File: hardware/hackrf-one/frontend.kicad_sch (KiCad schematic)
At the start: 149 parts, among them J10 GND_CLIP, J2 RF-SHIELD-FRAME, J3 RF-SHIELD-COVER, J4 MOUNTING_HOLE, J5 MOUNTING_HOLE, J6 MOUNTING_HOLE, J7 MOUNTING_HOLE, J8 MOUNTING_HOLE, J9 MOUNTING_HOLE, P13 GPO1, P17 GPO6, P19 GPO3, P21 REF_IN, P27 MIXER_SDATA, P31 MIXER_SCLK, P32 MIXER_ENX, P33 MIXER_RESETX, P34 MIX_BYPASS, P35 !MIX_BYPASS, P4 ANTENNA, P43 RX, P44 HP, P45 LP, P46 TX_MIX_BP, P47 RX_MIX_BP, P48 TX_AMP, P49 RX_AMP, P50 AMP_BYPASS, P51 !TX_AMP_PWR, P52 !RX_AMP_PWR, P6 GPO4, P7 GPO2, Q4 MOSFET_P, T1 MIX_IN_BALUN, T2 MIX_OUT_BALUN, U1 SKY13453, U10 SKY13453, U11 SKY13453, U12 SKY13317, U13 TRF37B73, U14 SKY13317, U2 SKY13453, U25 TRF37B73, U3 RX_LOWPASS_FILTER, U4 RFFC5072, U5 SKY13453, U6 SKY13453, U7 SKY13453, U8 RX_HIGHPASS_FILTER, U9 SKY13317

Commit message: Fixed minor DRCs
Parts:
- P4: footprint hackrf:GSG-SMA-73251-2120 -> gsg-modules:SMA-73251-2120
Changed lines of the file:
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@@
 			)
 		)
-		(property "Footprint" "hackrf:GSG-SMA-73251-2120"
+		(property "Footprint" "gsg-modules:SMA-73251-2120"
 			(at 414.02 214.63 0)
 			(effects

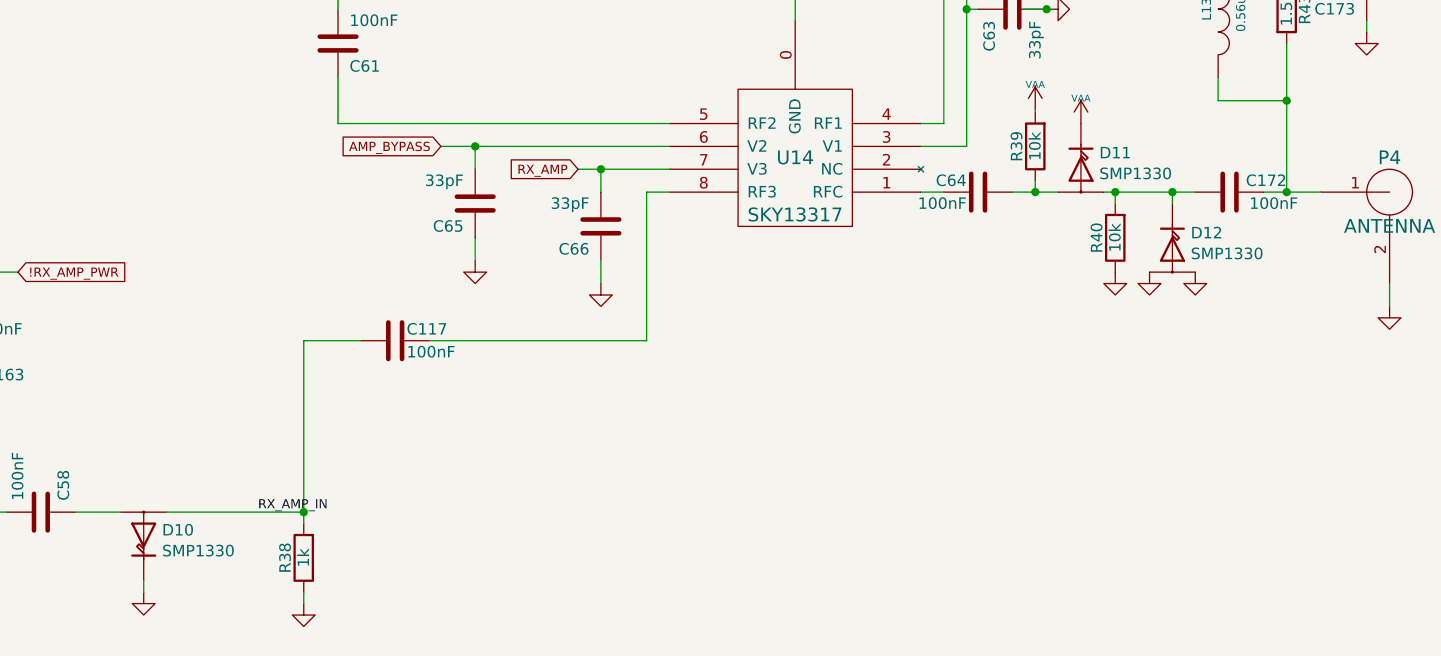
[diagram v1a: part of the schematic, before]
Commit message: Changed from SMP1330 to CLA4611 to improve performance to 6GHz
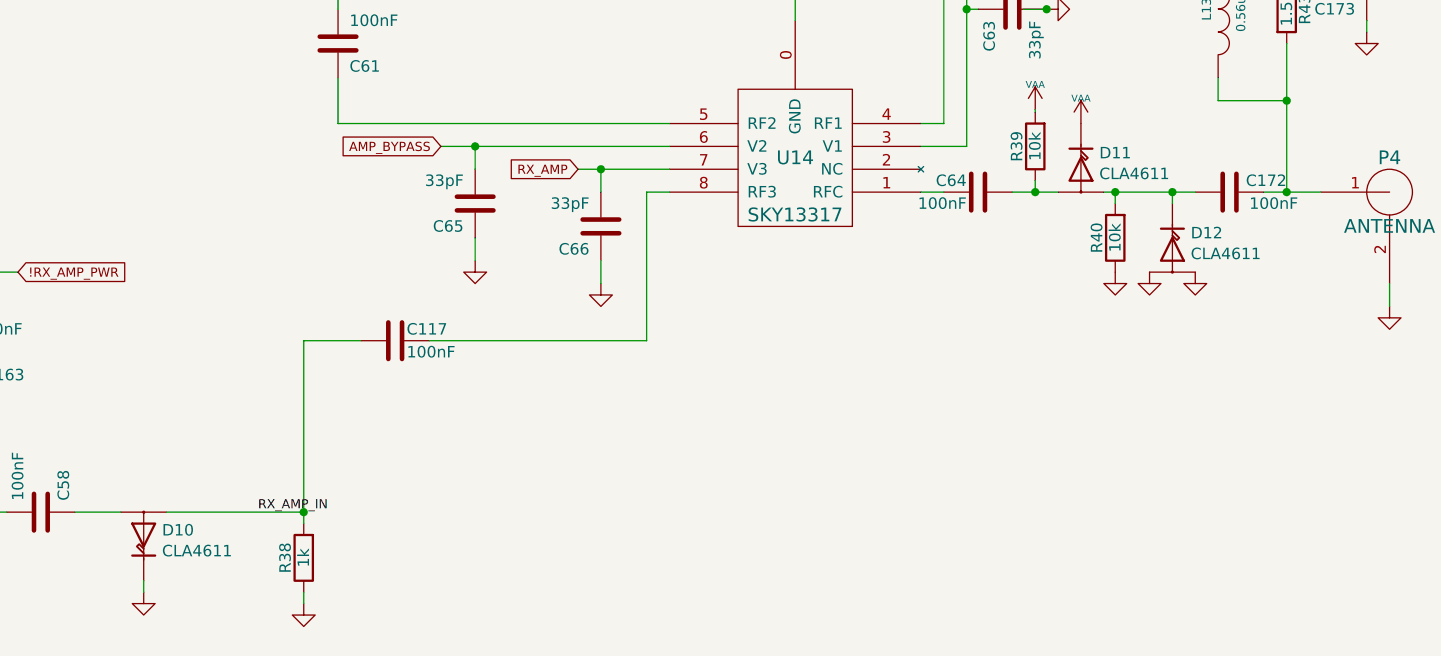
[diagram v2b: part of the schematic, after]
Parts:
- D10, D11, D12: value SMP1330 -> CLA4611; footprint gsg-modules:SMP1330-085LF -> gsg-modules:SkyworksLimiterDiode; symbol hackrf-one:D_Limiter_DualAn-hackrf -> gsg-kicad-lib:CLA4611_Limiter_Diode; Part Number SMP1330-085LF -> CLA4611-085LF
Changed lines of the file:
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@@
 	)
 	(symbol
-		(lib_id "hackrf-one:D_Limiter_DualAn-hackrf")
+		(lib_id "gsg-kicad-lib:CLA4611_Limiter_Diode")
 		(at 379.73 212.09 270)
 		(unit 1)
@@
 			)
 		)
-		(property "Value" "SMP1330"
+		(property "Value" "CLA4611"
 			(at 381.762 212.598 90)
 			(effects
@@
 			)
 		)
-		(property "Footprint" "gsg-modules:SMP1330-085LF"
+		(property "Footprint" "gsg-modules:SkyworksLimiterDiode"
 			(at 379.73 212.09 0)
 			(effects
@@
 		)
 		(property "Description" "Limiter Diode"
-			(at 379.73 212.09 90)
+			(at 379.73 212.09 0)
 			(effects
 				(font
@@
 			)
 		)
-		(property "Part Number" "SMP1330-085LF"
+		(property "Part Number" "CLA4611-085LF"
 			(at 379.73 212.09 90)
 			(effects
@@
 	)
 	(symbol
-		(lib_id "hackrf-one:D_Limiter_DualAn-hackrf")
+		(lib_id "gsg-kicad-lib:CLA4611_Limiter_Diode")
 		(at 389.89 220.98 270)
 		(unit 1)
@@
 			)
 		)
-		(property "Value" "SMP1330"
+		(property "Value" "CLA4611"
 			(at 391.922 221.488 90)
 			(effects
@@
 			)
 		)
-		(property "Footprint" "gsg-modules:SMP1330-085LF"
+		(property "Footprint" "gsg-modules:SkyworksLimiterDiode"
 			(at 389.89 220.98 0)
 			(effects
@@
 		)
 		(property "Description" "Limiter Diode"
-			(at 389.89 220.98 90)
+			(at 389.89 220.98 0)
 			(effects
 				(font
@@
 			)
 		)
-		(property "Part Number" "SMP1330-085LF"
+		(property "Part Number" "CLA4611-085LF"
 			(at 389.89 220.98 90)
 			(effects
@@
 	)
 	(symbol
-		(lib_id "hackrf-one:D_Limiter_DualAn-hackrf")
+		(lib_id "gsg-kicad-lib:CLA4611_Limiter_Diode")
 		(at 275.59 252.73 90)
 		(unit 1)
@@
 			)
 		)
-		(property "Value" "SMP1330"
+		(property "Value" "CLA4611"
 			(at 277.622 254.508 90)
 			(effects
@@
 			)
 		)
-		(property "Footprint" "gsg-modules:SMP1330-085LF"
+		(property "Footprint" "gsg-modules:SkyworksLimiterDiode"
 			(at 275.59 252.73 0)
 			(effects
@@
 		)
 		(property "Description" "Limiter Diode"
-			(at 275.59 252.73 90)
+			(at 275.59 252.73 0)
 			(effects
 				(font
@@
 			)
 		)
-		(property "Part Number" "SMP1330-085LF"
+		(property "Part Number" "CLA4611-085LF"
 			(at 275.59 252.73 90)
 			(effects

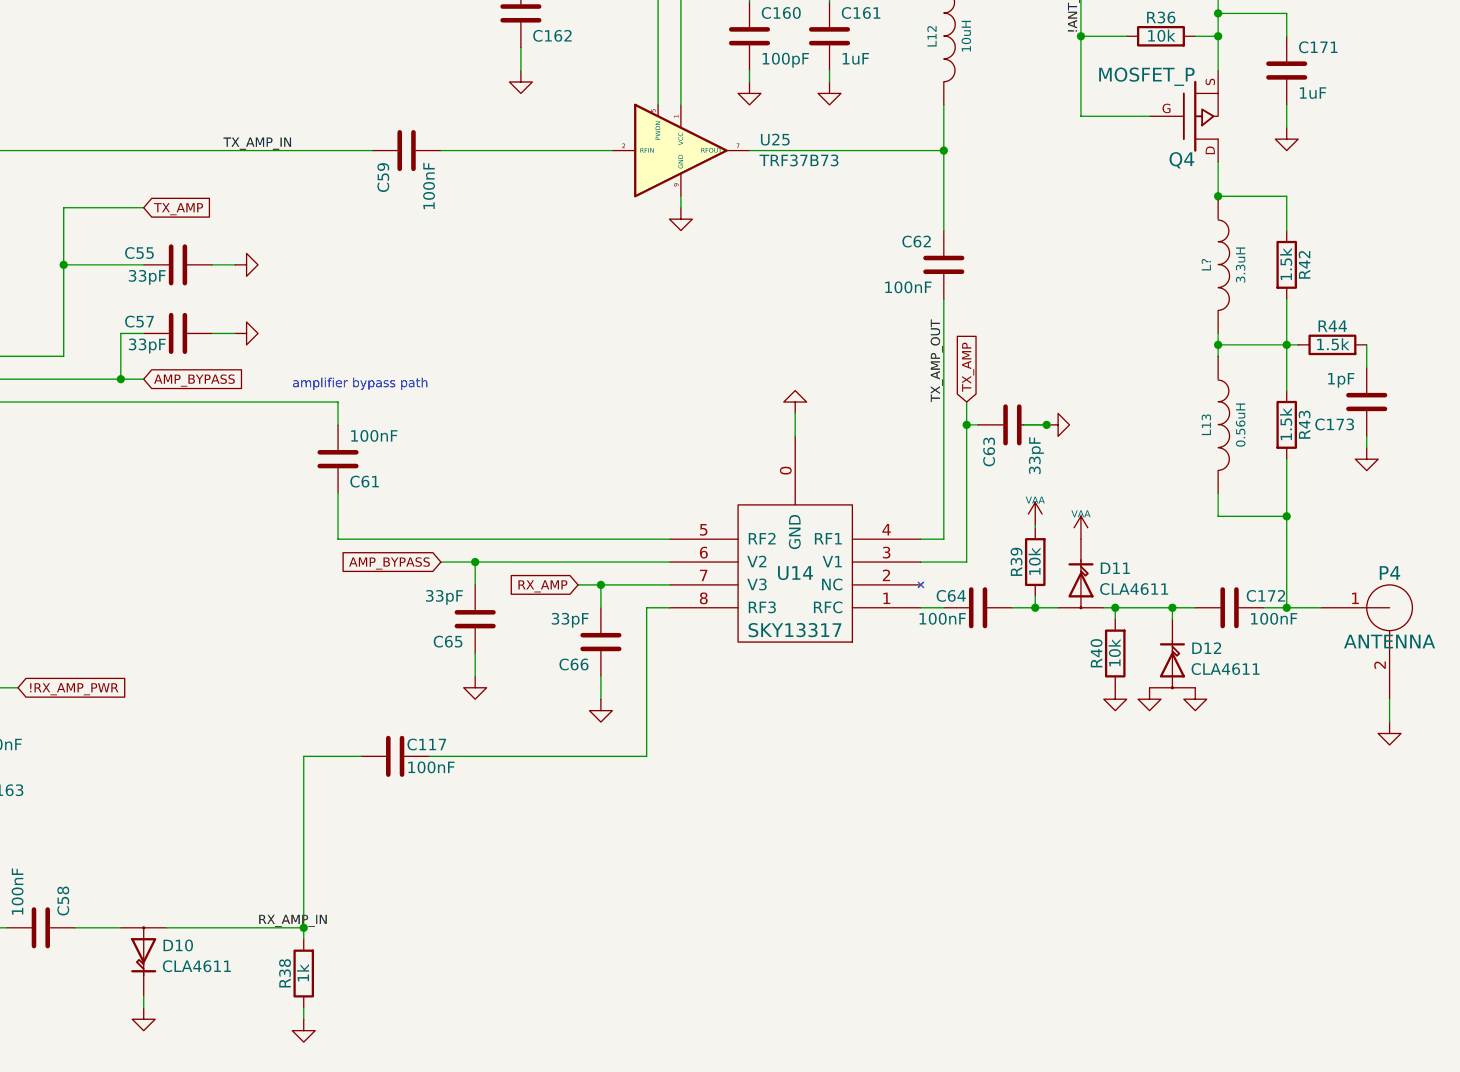
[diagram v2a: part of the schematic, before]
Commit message: Changed limiter to CLA4611. Added Schottky bias tee diode
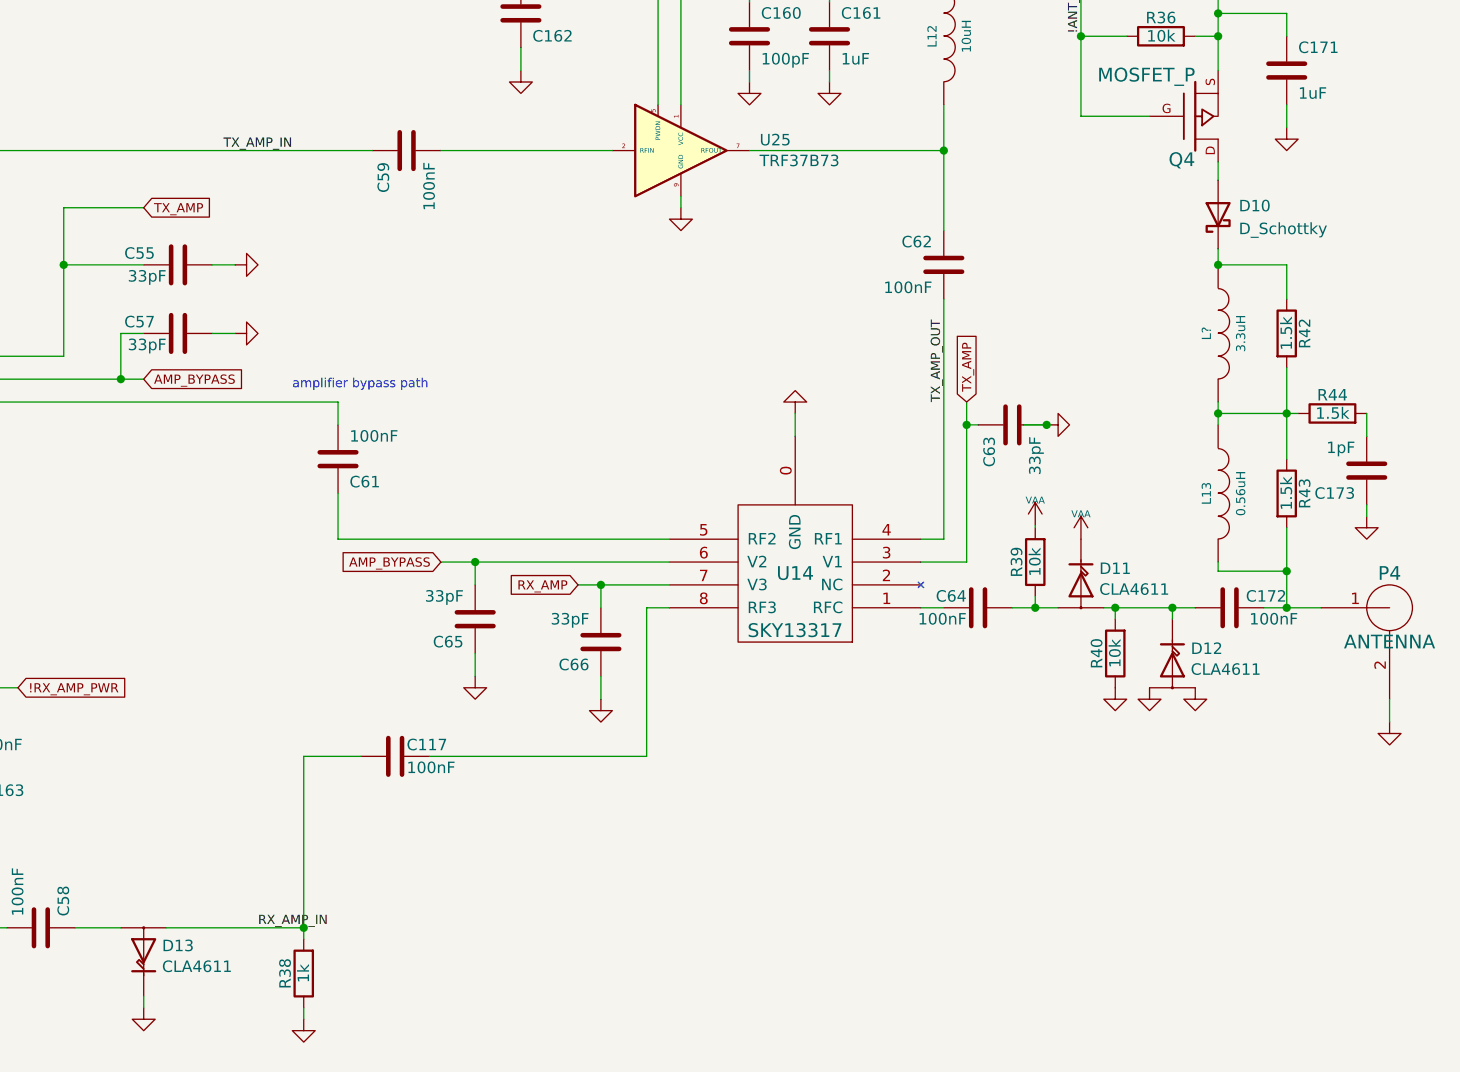
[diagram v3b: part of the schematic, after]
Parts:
- added D10: D_Schottky, gsg-modules:DSN1006-2, symbol Device:D_Schottky
- renumbered D10 to D13
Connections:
- net at L?.1, R42.1: now also D10.1 (K); no longer Q4.D
- new net: D10.2 (A), Q4.D
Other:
- moved on the sheet: C173, L13, L?, R42, R43, R44

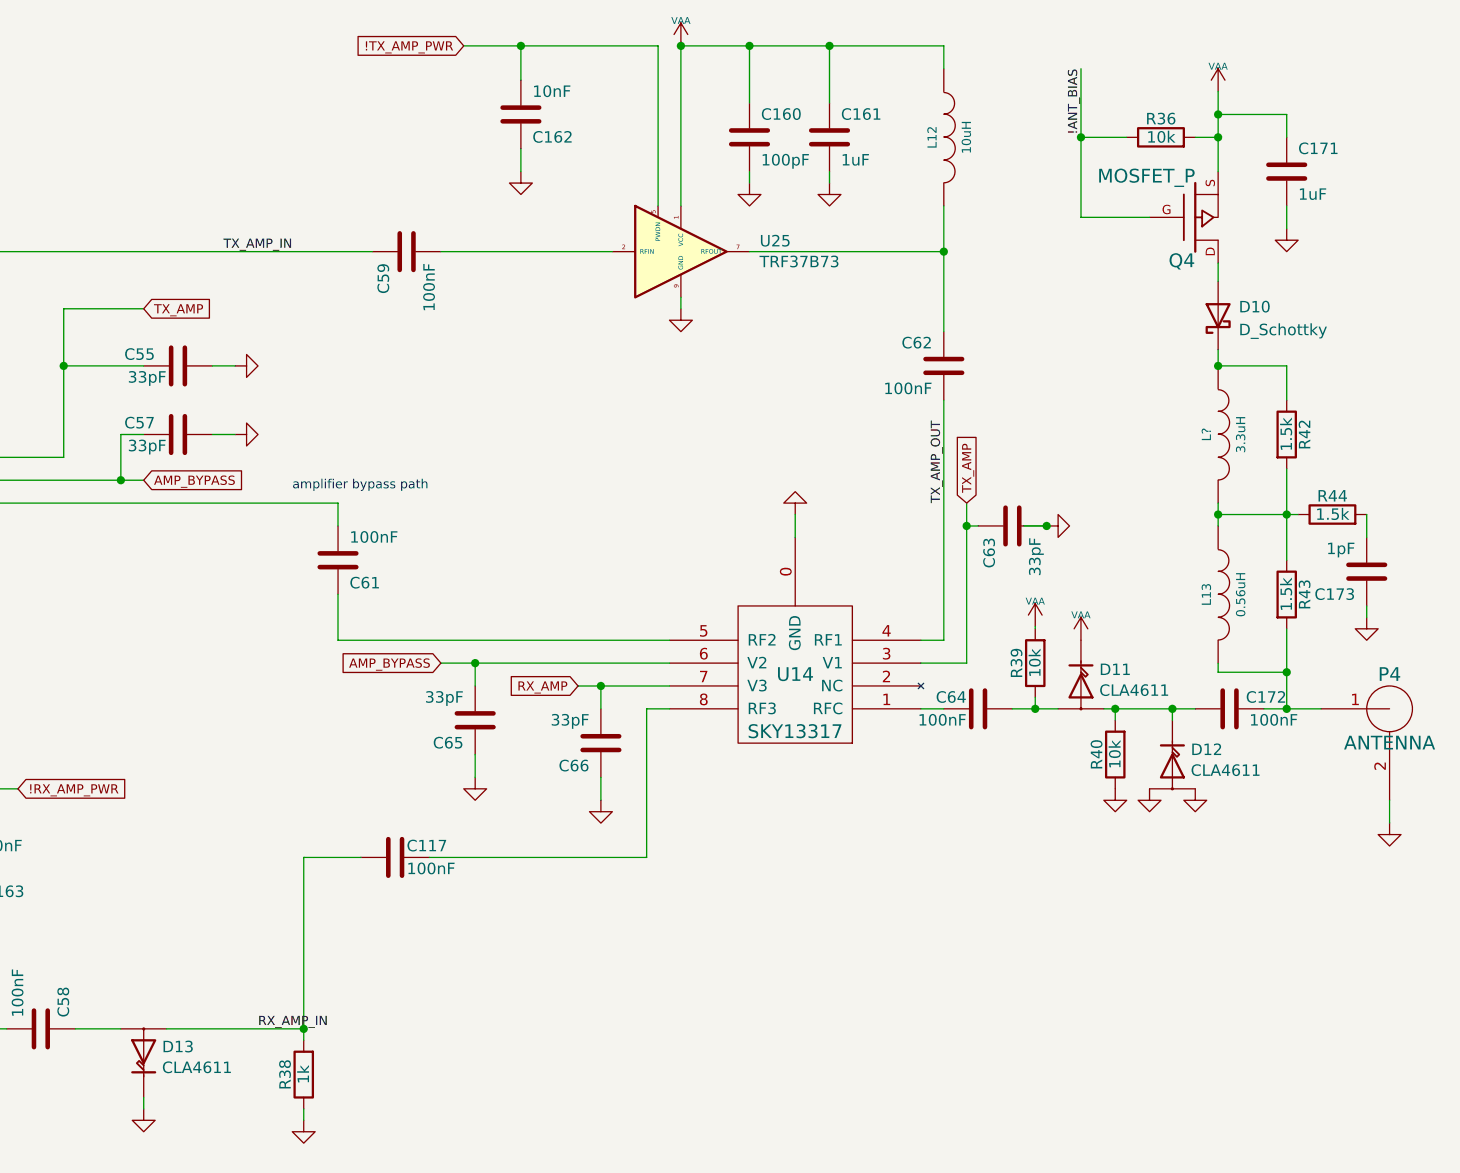
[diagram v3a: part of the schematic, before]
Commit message: Updated to move USB-C connector to save location as OpenSourceSDRLab's R10C
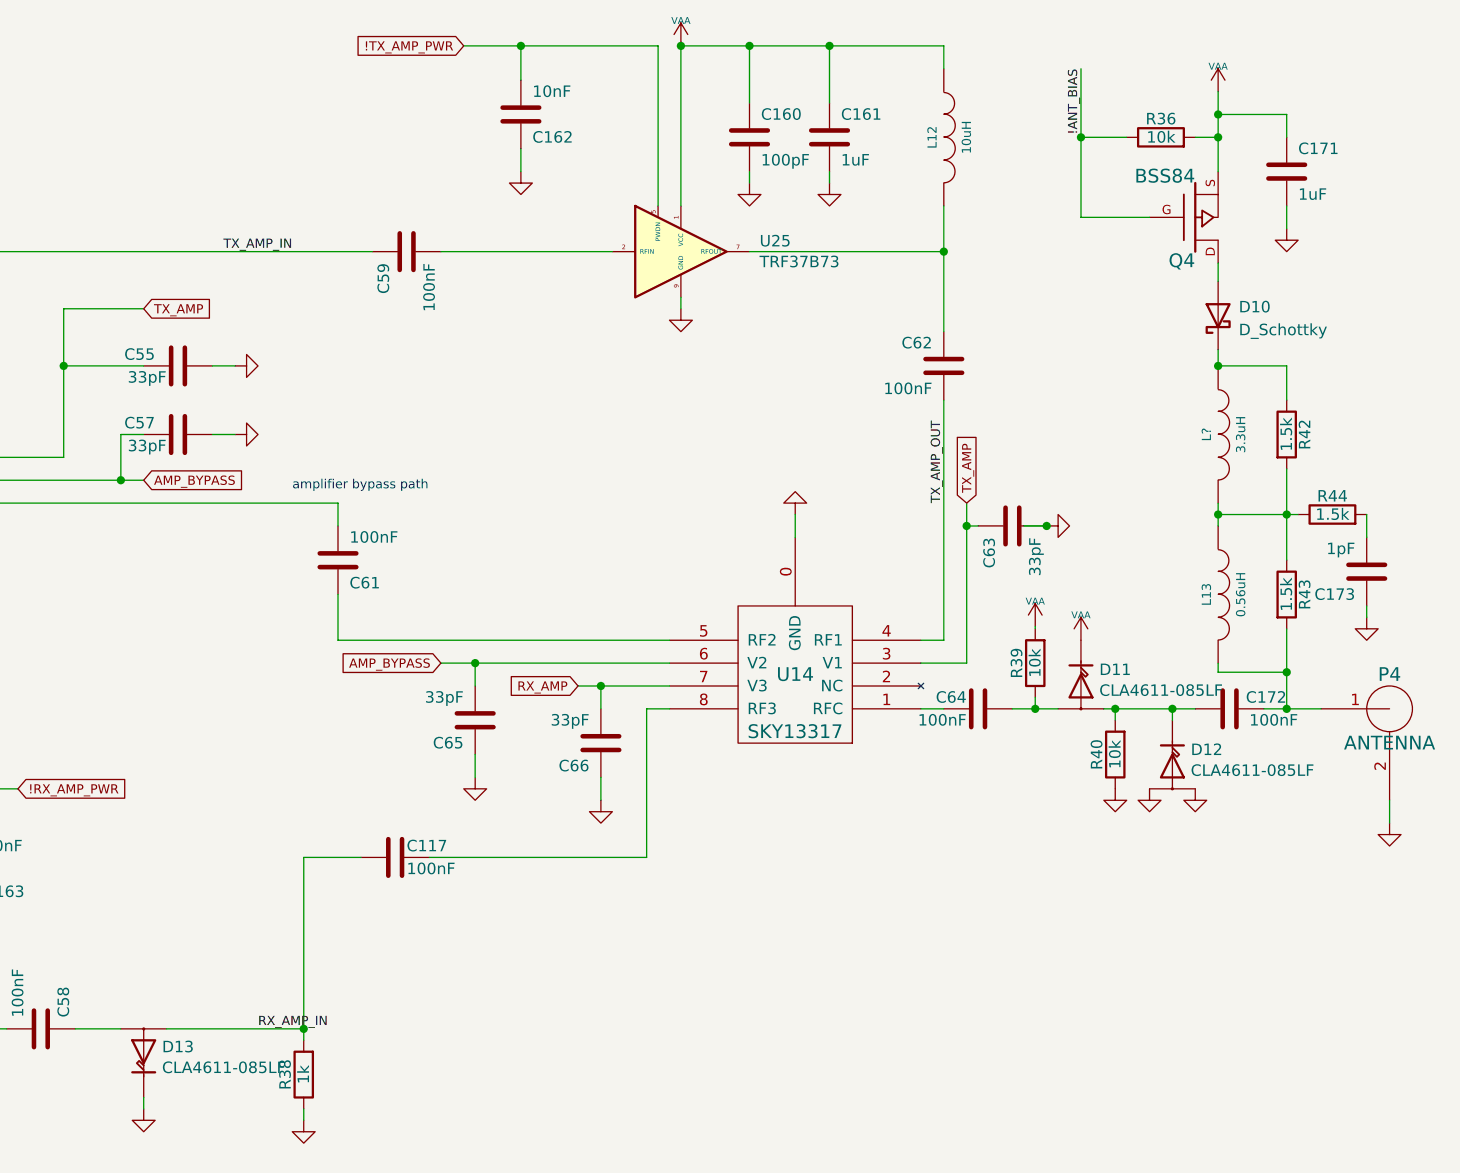
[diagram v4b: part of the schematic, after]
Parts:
- D11, D12, D13: value CLA4611 -> CLA4611-085LF
- Q4: value MOSFET_P -> BSS84
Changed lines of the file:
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@@
 			)
 		)
-		(property "Value" "MOSFET_P"
+		(property "Value" "BSS84"
 			(at 392.43 155.448 0)
 			(effects
@@
 			)
 		)
-		(property "Value" "CLA4611"
+		(property "Value" "CLA4611-085LF"
 			(at 381.762 212.598 90)
 			(effects
@@
 			)
 		)
-		(property "Value" "CLA4611"
+		(property "Value" "CLA4611-085LF"
 			(at 391.922 221.488 90)
 			(effects
@@
 			)
 		)
-		(property "Value" "CLA4611"
+		(property "Value" "CLA4611-085LF"
 			(at 277.622 254.508 90)
 			(effects
